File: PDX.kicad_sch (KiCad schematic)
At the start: 104 parts, among them Q1 BS170, Q2 BS170, Q3 BS170, Q4 BS170, Q5 BC547, Q6 BC547, U1 CD2003GB_GP, U2 SI5351_Module, U3 74ACT244, U6 LM393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

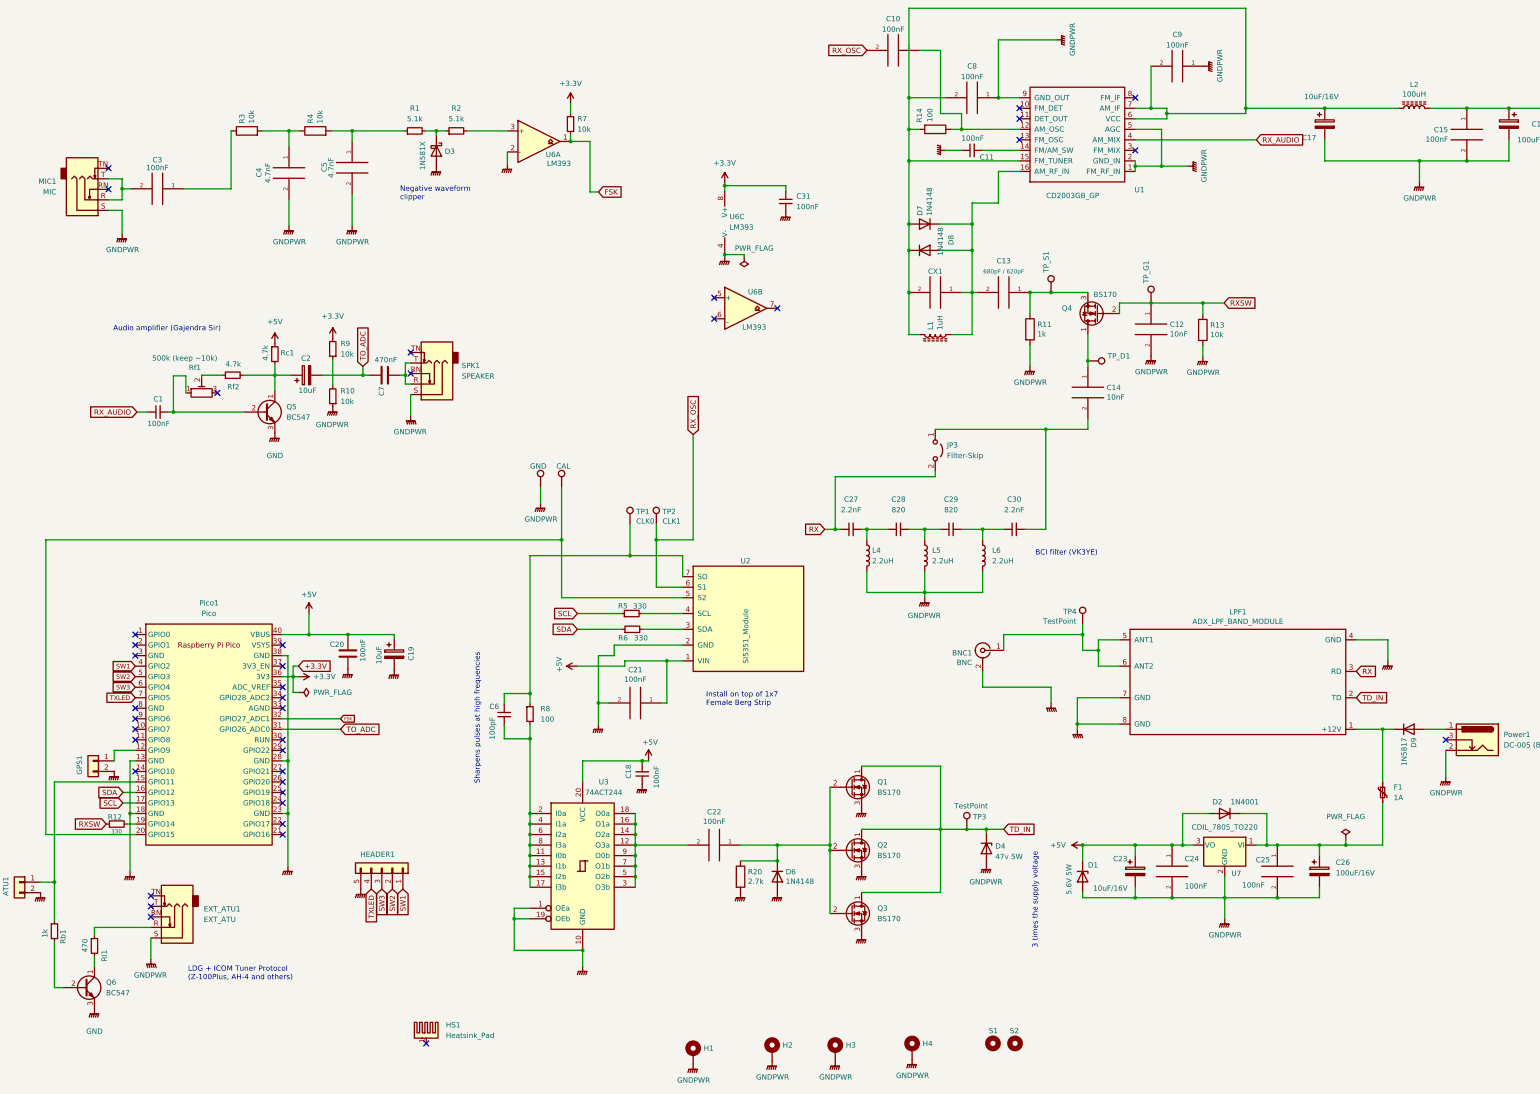
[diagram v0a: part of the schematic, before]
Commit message: PCB v0.2 + Initial firmware
PCB changes:

- Use `TO-92_HandSolder` footprint

- Use (optional) sockets for BS170 finals!

- Add `Test Point` for comparator output

- Remove onboard heatsink - it is not needed

- Provide +5V on the output header

- Make the +5V supply to Pico optional via a jumper

  - This enables external CAT control of Pico via USB

- Tie the unused LM393 inputs to ground

- Dual-input (+5V directly at VSYS and +5V from USB) power supply
  mechanism for Pico (similar to what Arduino Nano has).

Code changes:

- Initial firmware with CAT support (WSJT-X / 'FT8 Radio' Android app)

- The `freqPIO` stuff will be enabled later after testing
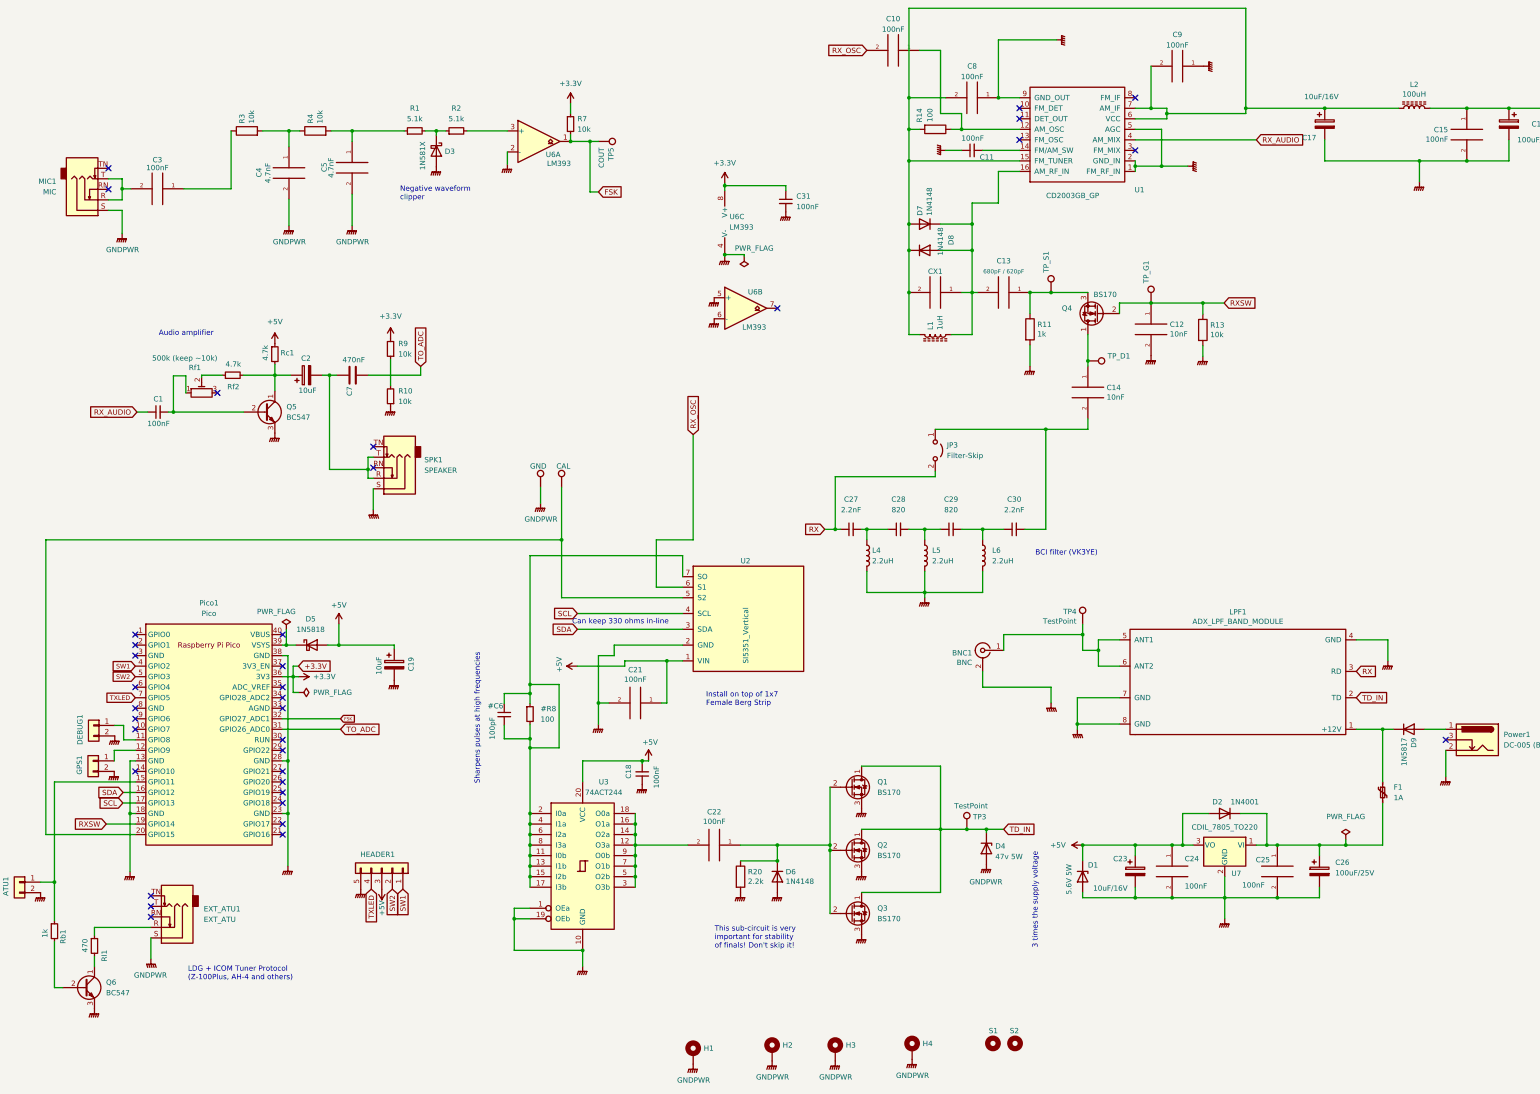
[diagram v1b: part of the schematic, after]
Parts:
- removed C20: 100nF, Capacitor_THT:C_Disc_D3.0mm_W2.0mm_P2.50mm, symbol Device:C
- removed HS1: Heatsink_Pad, footprints:ThermalPad_Final, symbol Mechanical:Heatsink_Pad
- removed R12, R5, R6: 330, Resistor_THT:R_Axial_DIN0204_L3.6mm_D1.6mm_P1.90mm_Vertical, symbol Device:R_Small
- removed TP1: CLK0, TestPoint:TestPoint_THTPad_2.0x2.0mm_Drill1.0mm, symbol Connector:TestPoint
- removed TP2: CLK1, TestPoint:TestPoint_THTPad_2.0x2.0mm_Drill1.0mm, symbol Connector:TestPoint
- added D5: 1N5818, Diode_THT:D_DO-41_SOD81_P2.54mm_Vertical_KathodeUp, symbol Diode:1N5818
- added DEBUG1: Conn_01x02, Connector_PinHeader_2.54mm:PinHeader_1x02_P2.54mm_Vertical, symbol Connector_Generic:Conn_01x02
- added TP5: COUT, TestPoint:TestPoint_THTPad_2.0x2.0mm_Drill1.0mm, symbol Connector:TestPoint
- C26: value 100uF/16V -> 100uF/25V
- D6: footprint Diode_THT:D_DO-35_SOD27_P2.54mm_Vertical_AnodeUp -> Diode_THT:D_DO-35_SOD27_P2.54mm_Vertical_KathodeUp
- Q1, Q2, Q3: footprint Package_TO_SOT_THT:TO-92_Inline -> Connector_PinSocket_2.54mm:PinSocket_1x03_P2.54mm_Vertical
- Q4: footprint Package_TO_SOT_THT:TO-92_Inline -> Package_TO_SOT_THT:TO-92_HandSolder
- R20: value 2.7k -> 2.2k
- U2: value SI5351_Module -> SI5351_Vertical
- renumbered C6 to #C6, R8 to #R8
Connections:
- net +5V: now also HEADER1.3 (Pin_3), D5.2 (A); no longer Pico1.40 (VBUS)
- net FSK: now also TP5.1
- net GNDPWR: now also U6.5 (+), U6.6 (-), DEBUG1.2 (Pin_2)
- net RXSW: now also Pico1.19 (GPIO14)
- net SCL: now also U2.4 (SCL)
- net SDA: now also U2.3 (SDA)
- net TO_ADC: now also C7.1; no longer C2.2, C7.2
- net at #C6.1, #R8.1, U2.7 (SO): now also #C6.2, #R8.2, U3.11 (I0b), U3.13 (I1b), U3.15 (I2b), U3.17 (I3b), U3.2 (I0a), U3.4 (I1a), U3.6 (I2a), U3.8 (I3a)
- net at SPK1.R, SPK1.T: now also C2.2, C7.2; no longer C7.1
- net at Pico1.11 (GPIO8): now also DEBUG1.1 (Pin_1)
- net at Pico1.39 (VSYS): now also D5.1 (K)
- net SW3: no longer names the net of Pico1.6 (GPIO4)
- net SW3: no longer HEADER1.3 (Pin_3)
- no-connect marks 39 -> 36
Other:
- note added: "Audio amplifier"
- note added: "Can keep 330 ohms in-line"
- note added: "This sub-circuit is very important for stability of finals! Don't skip it!"
- note removed: "Audio amplifier (Gajendra Sir)"
- moved on the sheet: C19, C7, R10, R9, SPK1
